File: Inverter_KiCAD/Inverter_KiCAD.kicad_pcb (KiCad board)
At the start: 2 copper layers, 46.8 x 6.8 mm, 139 parts, among them J1 PX0580-PC-12132, J2 Conn_ST_STDC14, J3 Conn_01x04, J4 Conn_01x05, J5 USB_C_Receptacle_USB2.0, Q1 HCPL-315J-500E, Q10 HCPL-315J-500E, Q2 IRF540N, Q3 IRF540N, Q4 IRF540N, Q5 IRF540N, Q6 HCPL-315J-500E, Q7 IRF540N, Q8 IRF540N, Q9 BUK9637-100E, SW1 SW_Push, SW2 SW_Push, SW3 SW_Push, SW4 SW_Push, SW5 SW_Push, U1 MPRB2415S-6W, U10 MPRB2415S-6W, U12 MPRB2415S-6W, U13 MP-LD30-23B12R2, U14 AZ1117-3.3, U15 HCPL-7800A, U16 HCPL-7800A, U17 GO 10-SME/SP3, U18 STM32G474RETx, U19 GO 10-SME/SP3, U2 MPRB2415S-6W, U20 USBLC6-2SC6, U22 ACPL-077L, U3 HCPL-7800A, U4 MPRB2415S-6W, U5 MPRB2415S-6W, U6 GO 10-SME/SP3, U8 HCPL-7800A, U9 GO 10-SME/SP3

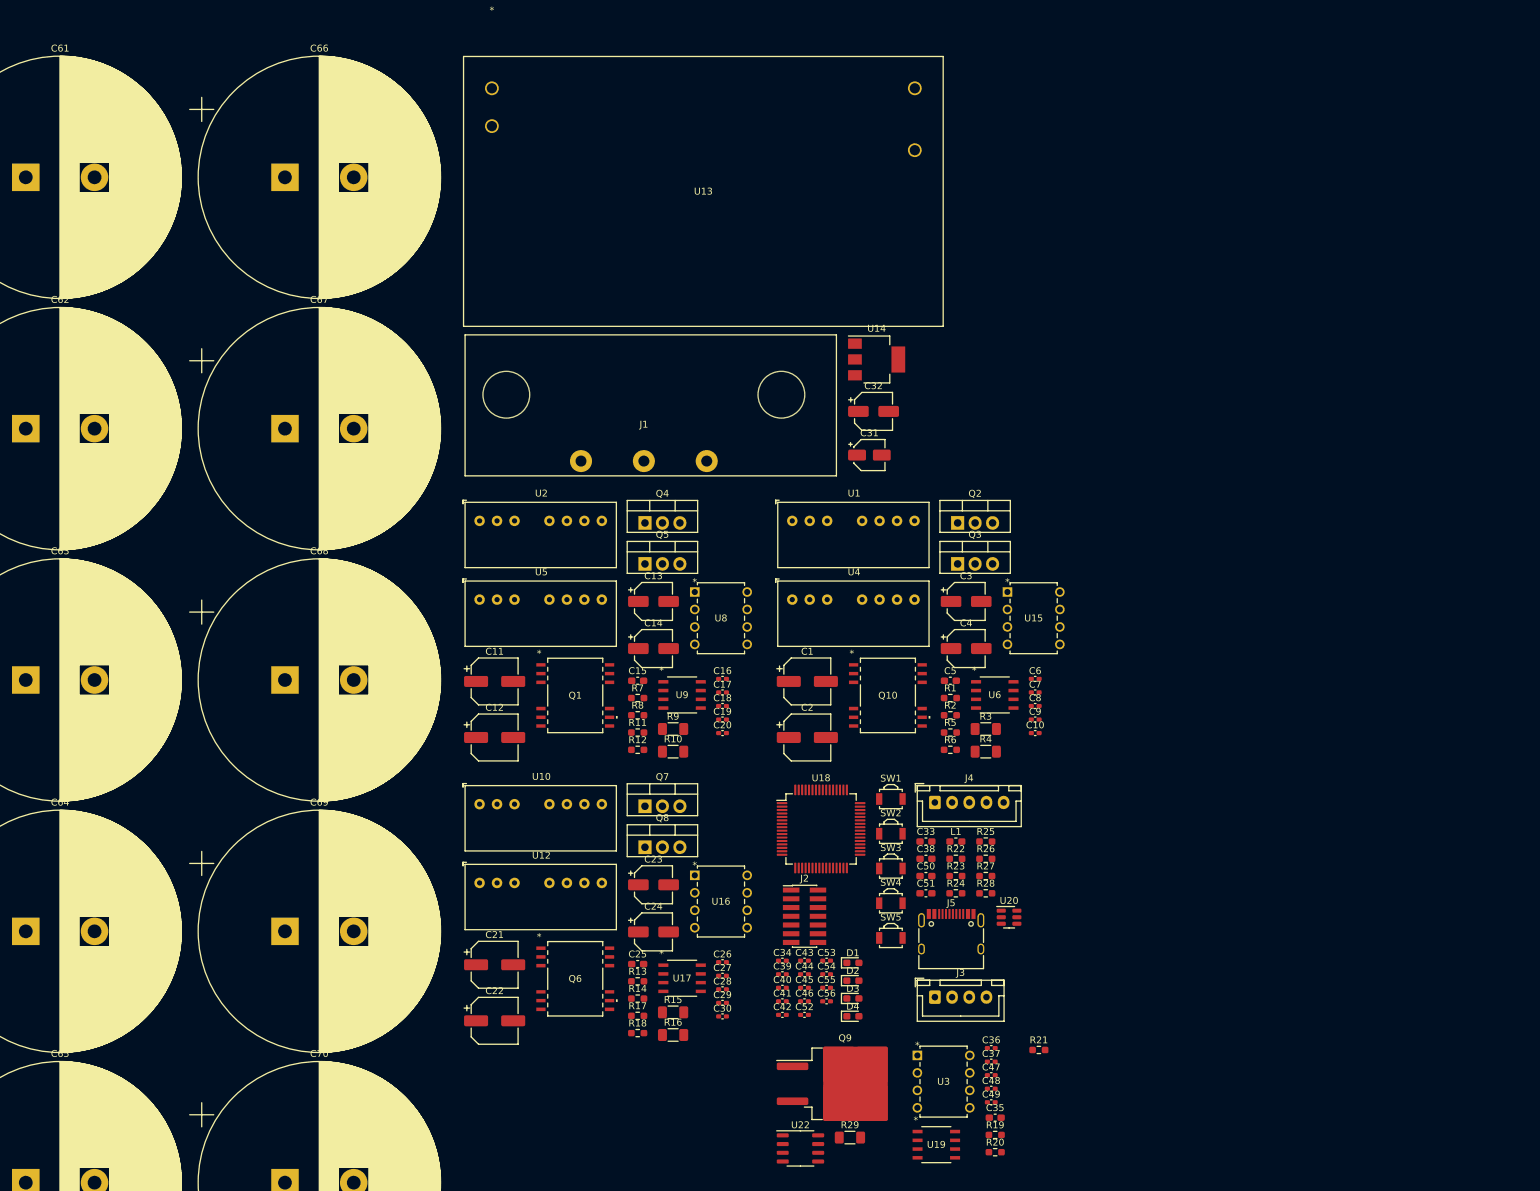
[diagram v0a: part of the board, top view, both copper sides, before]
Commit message: clear schematic errors
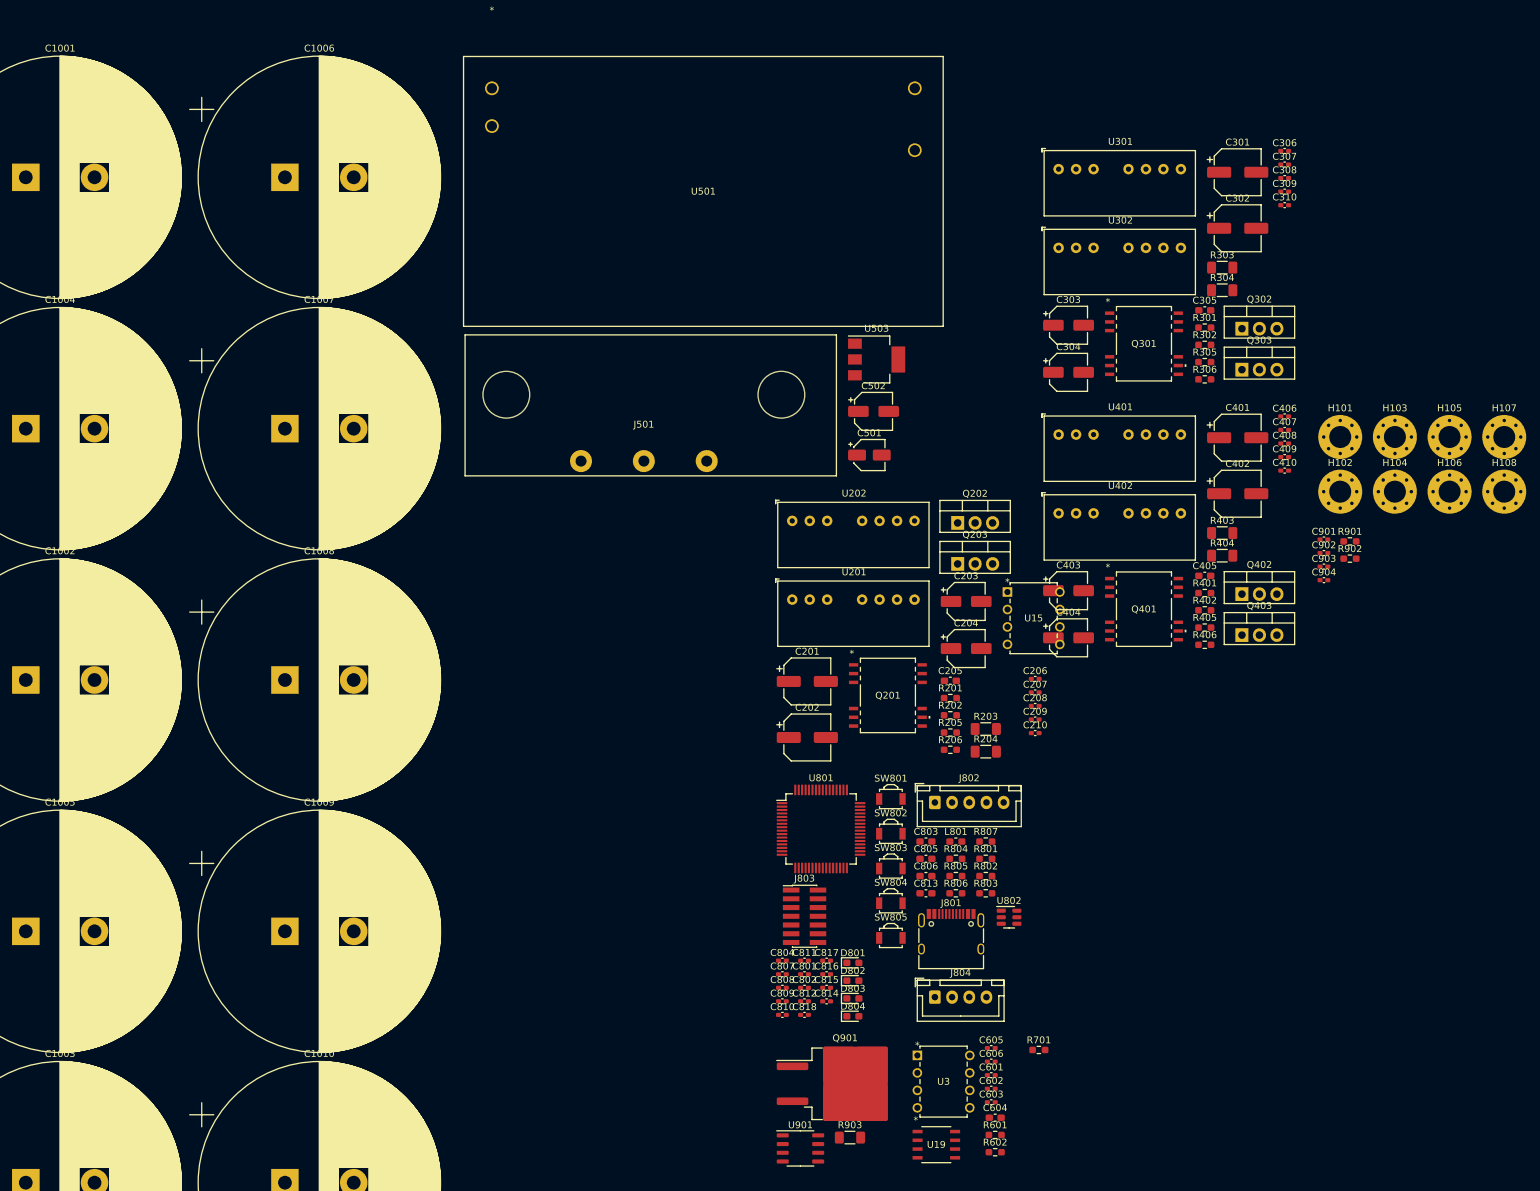
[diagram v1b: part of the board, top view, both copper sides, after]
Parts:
- removed C11, C12, C21, C22: 100u, Capacitor_SMD:CP_Elec_6.3x7.7
- removed C13, C14, C23, C24: 22u, Capacitor_SMD:CP_Elec_5x5.4
- removed C15, C25: C_Small, Capacitor_SMD:C_0603_1608Metric_Pad1.08x0.95mm_HandSolder
- removed C16, C17, C26, C27: 100n, Capacitor_SMD:C_0402_1005Metric_Pad0.74x0.62mm_HandSolder
- removed C18, C19, C20, C28, C29, C30: 4.7n, Capacitor_SMD:C_0402_1005Metric_Pad0.74x0.62mm_HandSolder
- removed Q1, Q6: HCPL-315J-500E, Custom:SO-16_HCPL-315J_BRA
- removed Q4, Q5, Q7, Q8: IRF540N, Package_TO_SOT_THT:TO-220-3_Vertical
- removed R10, R15, R16, R9: 30, Resistor_SMD:R_1206_3216Metric_Pad1.30x1.75mm_HandSolder
- removed R11, R12, R17, R18: R_Small, Resistor_SMD:R_0603_1608Metric_Pad0.98x0.95mm_HandSolder
- removed R13, R14, R7, R8: 170, Resistor_SMD:R_0603_1608Metric_Pad0.98x0.95mm_HandSolder
- removed U10, U12, U2, U5: MPRB2415S-6W, Custom:MPRB2415S
- removed U16, U8: HCPL-7800A, Custom:HCPL-7800A
- removed U17, U6, U9: GO 10-SME/SP3, Custom:SOIC8-GO-SME&slash_SP3_LEM
- added C301: 100u, Capacitor_SMD:CP_Elec_6.3x7.7, F.Cu at (184.9, 27.1)
- added C302: 100u, Capacitor_SMD:CP_Elec_6.3x7.7, F.Cu at (184.9, 35.2)
- added C303: 22u, Capacitor_SMD:CP_Elec_5x5.4, F.Cu at (160.3, 49.3)
- added C304: 22u, Capacitor_SMD:CP_Elec_5x5.4, F.Cu at (160.3, 56.2)
- added C305: 10n, Capacitor_SMD:C_0603_1608Metric_Pad1.08x0.95mm_HandSolder, F.Cu at (180.1, 47.1)
- added C306: 100n, Capacitor_SMD:C_0402_1005Metric_Pad0.74x0.62mm_HandSolder, F.Cu at (191.7, 24.0)
- added C307: 100n, Capacitor_SMD:C_0402_1005Metric_Pad0.74x0.62mm_HandSolder, F.Cu at (191.7, 25.9)
- added C308: 4.7n, Capacitor_SMD:C_0402_1005Metric_Pad0.74x0.62mm_HandSolder, F.Cu at (191.7, 27.9)
- added C309: 4.7n, Capacitor_SMD:C_0402_1005Metric_Pad0.74x0.62mm_HandSolder, F.Cu at (191.7, 29.9)
- added C310: 4.7n, Capacitor_SMD:C_0402_1005Metric_Pad0.74x0.62mm_HandSolder, F.Cu at (191.7, 31.9)
- added C401: 100u, Capacitor_SMD:CP_Elec_6.3x7.7, F.Cu at (184.9, 65.7)
- added C402: 100u, Capacitor_SMD:CP_Elec_6.3x7.7, F.Cu at (184.9, 73.8)
- added C403: 22u, Capacitor_SMD:CP_Elec_5x5.4, F.Cu at (160.3, 87.9)
- added C404: 22u, Capacitor_SMD:CP_Elec_5x5.4, F.Cu at (160.3, 94.8)
- added C405: 10n, Capacitor_SMD:C_0603_1608Metric_Pad1.08x0.95mm_HandSolder, F.Cu at (180.1, 85.7)
- added C406: 100n, Capacitor_SMD:C_0402_1005Metric_Pad0.74x0.62mm_HandSolder, F.Cu at (191.7, 62.6)
- added C407: 100n, Capacitor_SMD:C_0402_1005Metric_Pad0.74x0.62mm_HandSolder, F.Cu at (191.7, 64.5)
- added C408: 4.7n, Capacitor_SMD:C_0402_1005Metric_Pad0.74x0.62mm_HandSolder, F.Cu at (191.7, 66.5)
- added C409: 4.7n, Capacitor_SMD:C_0402_1005Metric_Pad0.74x0.62mm_HandSolder, F.Cu at (191.7, 68.5)
- added C410: 4.7n, Capacitor_SMD:C_0402_1005Metric_Pad0.74x0.62mm_HandSolder, F.Cu at (191.7, 70.5)
- added C901: 100n, Capacitor_SMD:C_0402_1005Metric_Pad0.74x0.62mm_HandSolder, F.Cu at (197.4, 80.5)
- added C902: 100n, Capacitor_SMD:C_0402_1005Metric_Pad0.74x0.62mm_HandSolder, F.Cu at (197.4, 82.4)
- added C903: 1u, Capacitor_SMD:C_0402_1005Metric_Pad0.74x0.62mm_HandSolder, F.Cu at (197.4, 84.4)
- added C904: 1n, Capacitor_SMD:C_0402_1005Metric_Pad0.74x0.62mm_HandSolder, F.Cu at (197.4, 86.4)
- added H101: MountingHole_Pad, MountingHole:MountingHole_3.2mm_M3_Pad_Via, F.Cu at (199.8, 65.6)
- added H102: MountingHole_Pad, MountingHole:MountingHole_3.2mm_M3_Pad_Via, F.Cu at (199.8, 73.5)
- added H103: MountingHole_Pad, MountingHole:MountingHole_3.2mm_M3_Pad_Via, F.Cu at (207.8, 65.6)
- added H104: MountingHole_Pad, MountingHole:MountingHole_3.2mm_M3_Pad_Via, F.Cu at (207.8, 73.5)
- added H105: MountingHole_Pad, MountingHole:MountingHole_3.2mm_M3_Pad_Via, F.Cu at (215.7, 65.6)
- added H106: MountingHole_Pad, MountingHole:MountingHole_3.2mm_M3_Pad_Via, F.Cu at (215.7, 73.5)
- added H107: MountingHole_Pad, MountingHole:MountingHole_3.2mm_M3_Pad_Via, F.Cu at (223.7, 65.6)
- added H108: MountingHole_Pad, MountingHole:MountingHole_3.2mm_M3_Pad_Via, F.Cu at (223.7, 73.5)
- added Q301: HCPL-315J-500E, Custom:SO-16_HCPL-315J_BRA, F.Cu at (171.3, 52.0)
- added Q302: IRF540N, Package_TO_SOT_THT:TO-220-3_Vertical, F.Cu at (185.5, 49.8)
- added Q303: IRF540N, Package_TO_SOT_THT:TO-220-3_Vertical, F.Cu at (185.5, 55.8)
- added Q401: HCPL-315J-500E, Custom:SO-16_HCPL-315J_BRA, F.Cu at (171.3, 90.6)
- added Q402: IRF540N, Package_TO_SOT_THT:TO-220-3_Vertical, F.Cu at (185.5, 88.4)
- added Q403: IRF540N, Package_TO_SOT_THT:TO-220-3_Vertical, F.Cu at (185.5, 94.4)
- added R301: 170, Resistor_SMD:R_0603_1608Metric_Pad0.98x0.95mm_HandSolder, F.Cu at (180.1, 49.7)
- added R302: 170, Resistor_SMD:R_0603_1608Metric_Pad0.98x0.95mm_HandSolder, F.Cu at (180.1, 52.2)
- added R303: 30, Resistor_SMD:R_1206_3216Metric_Pad1.30x1.75mm_HandSolder, F.Cu at (182.7, 40.9)
- added R304: 30, Resistor_SMD:R_1206_3216Metric_Pad1.30x1.75mm_HandSolder, F.Cu at (182.7, 44.2)
- added R305: 160k, Resistor_SMD:R_0603_1608Metric_Pad0.98x0.95mm_HandSolder, F.Cu at (180.1, 54.7)
- added R306: 1k, Resistor_SMD:R_0603_1608Metric_Pad0.98x0.95mm_HandSolder, F.Cu at (180.1, 57.2)
- added R401: 170, Resistor_SMD:R_0603_1608Metric_Pad0.98x0.95mm_HandSolder, F.Cu at (180.1, 88.3)
- added R402: 170, Resistor_SMD:R_0603_1608Metric_Pad0.98x0.95mm_HandSolder, F.Cu at (180.1, 90.8)
- added R403: 30, Resistor_SMD:R_1206_3216Metric_Pad1.30x1.75mm_HandSolder, F.Cu at (182.7, 79.5)
- added R404: 30, Resistor_SMD:R_1206_3216Metric_Pad1.30x1.75mm_HandSolder, F.Cu at (182.7, 82.8)
- added R405: 160k, Resistor_SMD:R_0603_1608Metric_Pad0.98x0.95mm_HandSolder, F.Cu at (180.1, 93.3)
- added R406: 1k, Resistor_SMD:R_0603_1608Metric_Pad0.98x0.95mm_HandSolder, F.Cu at (180.1, 95.8)
- added R901: 100, Resistor_SMD:R_0603_1608Metric_Pad0.98x0.95mm_HandSolder, F.Cu at (201.2, 80.7)
- added R902: 10k, Resistor_SMD:R_0603_1608Metric_Pad0.98x0.95mm_HandSolder, F.Cu at (201.2, 83.3)
- added U301: MPRB2415S-6W, Custom:MPRB2415S, F.Cu at (167.8, 26.6)
- added U302: MPRB2415S-6W, Custom:MPRB2415S, F.Cu at (167.8, 38.1)
- added U401: MPRB2415S-6W, Custom:MPRB2415S, F.Cu at (167.8, 65.2)
- added U402: MPRB2415S-6W, Custom:MPRB2415S, F.Cu at (167.8, 76.7)
- C205: renamed from C5; value C_Small -> 10n
- C604: renamed from C35; value C_Small -> 10n
- R205: renamed from R5; value R_Small -> 160k
- R206: renamed from R6; value R_Small -> 1k
- R601: renamed from R19; value R_Small -> 160k
- R602: renamed from R20; value R_Small -> 1k
- renumbered C61 to C1001, C63 to C1002, C65 to C1003, C62 to C1004, C64 to C1005, C66 to C1006, C67 to C1007, C68 to C1008, C69 to C1009, C70 to C1010, C1 to C201, C2 to C202, C3 to C203, C4 to C204, C6 to C206, C7 to C207, C8 to C208, C9 to C209, C10 to C210, C31 to C501, C32 to C502, C47 to C601, C48 to C602, C49 to C603, C36 to C605, C37 to C606, C44 to C801, C45 to C802, C33 to C803, C34 to C804, C38 to C805, C50 to C806, C39 to C807, C40 to C808, C41 to C809, C42 to C810, C43 to C811, C46 to C812, C51 to C813, C56 to C814, C55 to C815, C54 to C816, C53 to C817, C52 to C818, D1 to D801, D2 to D802, D3 to D803, D4 to D804, J1 to J501, J5 to J801, J4 to J802, J2 to J803, J3 to J804, L1 to L801, Q10 to Q201, Q2 to Q202, Q3 to Q203, Q9 to Q901, R1 to R201, R2 to R202, R3 to R203, R4 to R204, R21 to R701, R26 to R801, R27 to R802, R28 to R803, R22 to R804, R23 to R805, R24 to R806, R25 to R807, R29 to R903, SW1 to SW801, SW2 to SW802, SW3 to SW803, SW4 to SW804, SW5 to SW805, U4 to U201, U1 to U202, U13 to U501, U14 to U503, U18 to U801, U20 to U802, U22 to U901
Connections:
- net /MCU_STM32G474/Nucleo_Rx renamed /NUCLEO_TX
- net /MCU_STM32G474/Nucleo_Tx renamed /NUCLEO_RX
- C205 pad 1: Net-(U15-VIN+) -> Net-(U203-VIN+)
- C604 pad 1: Net-(U3-VIN+) -> Net-(U602-VIN+)
- R205 pad 1: /Arm_IRF540NBbF/V_Out -> /U_output
- R205 pad 2: Net-(U15-VIN+) -> Net-(U203-VIN+)
- R206 pad 1: Net-(U15-VIN+) -> Net-(U203-VIN+)
- R601 pad 2: Net-(U3-VIN+) -> Net-(U602-VIN+)
- R602 pad 1: Net-(U3-VIN+) -> Net-(U602-VIN+)

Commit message: end of sch, start pcb
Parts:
- removed U15, U3: HCPL-7800A, Custom:HCPL-7800A
- added C1201: 100n, Capacitor_SMD:C_0402_1005Metric_Pad0.74x0.62mm_HandSolder, F.Cu at (-58.4, 163.0)
- added D901: Red, LED_SMD:LED_0603_1608Metric_Pad1.05x0.95mm_HandSolder, F.Cu at (-80.9, 181.3)
- added D902: VS-15TQ060S-M3, Package_TO_SOT_SMD:TO-263-2, F.Cu at (-80.8, 173.8)
- added F501: Fuse, Custom:0031.8201, F.Cu at (-78.4, 149.2)
- added J101: Conn_02x19_Odd_Even, Connector_PinHeader_2.54mm:PinHeader_2x19_P2.54mm_Vertical, F.Cu at (-120.0, 146.2)
- added J103: Conn_02x19_Odd_Even, Connector_PinHeader_2.54mm:PinHeader_2x19_P2.54mm_Vertical, F.Cu at (-98.4, 145.3)
- added J1101: Conn_01x02, Connector_JST:JST_XH_B2B-XH-A_1x02_P2.50mm_Vertical, F.Cu at (-55.7, 171.0)
- added J1102: Conn_01x02, Connector_JST:JST_XH_B2B-XH-A_1x02_P2.50mm_Vertical, F.Cu at (-55.7, 178.8)
- added Q1101: SQ2310ES, Package_TO_SOT_SMD:SOT-23, F.Cu at (-47.3, 169.8)
- added R1101: 22, Resistor_SMD:R_0402_1005Metric_Pad0.72x0.64mm_HandSolder, F.Cu at (-48.1, 173.1)
- added R1102: 10k, Resistor_SMD:R_0402_1005Metric_Pad0.72x0.64mm_HandSolder, F.Cu at (-48.1, 175.0)
- added R1201: 200, Resistor_SMD:R_0402_1005Metric_Pad0.72x0.64mm_HandSolder, F.Cu at (-61.6, 163.0)
- added U1201: TCN75A, Package_SO:SOIC-8_3.9x4.9mm_P1.27mm, F.Cu at (-59.0, 158.8)
- added U203: HCPL-7800A, Custom:HCPL-7800A, F.Cu at (-70.3, 190.0)
- added U204: GO 10-SME/SP3, Custom:SOIC8-GO-SME&slash_SP3_LEM, F.Cu at (-67.6, 203.0)
- added U303: HCPL-7800A, Custom:HCPL-7800A, F.Cu at (-90.0, 190.5)
- added U304: GO 10-SME/SP3, Custom:SOIC8-GO-SME&slash_SP3_LEM, F.Cu at (-87.3, 203.4)
- added U403: HCPL-7800A, Custom:HCPL-7800A, F.Cu at (-70.3, 169.7)
- added U404: GO 10-SME/SP3, Custom:SOIC8-GO-SME&slash_SP3_LEM, F.Cu at (-67.6, 182.6)
- added U502: 173010542, Custom:173010578, F.Cu at (-87.4, 158.3)
- added U602: HCPL-7800A, Custom:HCPL-7800A, F.Cu at (-57.6, 195.6)
- added U701: 17791063215, Custom:17791063215, F.Cu at (-51.6, 148.3)
- added U902: TC1412, Package_SO:SOIC-8_3.9x4.9mm_P1.27mm, F.Cu at (-87.3, 183.2)
- added Y801: 16M, Custom:ABLS-7.3728MHZ-CL-RESR-A-1-G-F, F.Cu at (-51.5, 188.4)
- C205, C305, C405, C604, C805: footprint Capacitor_SMD:C_0603_1608Metric_Pad1.08x0.95mm_HandSolder -> Capacitor_SMD:C_0402_1005Metric_Pad0.74x0.62mm_HandSolder
- R201, R202, R205, R206, R301, R302, R305, R306, R401, R402, R405, R406, R601, R602, R701, R801, R802, R803, R804, R805, R806, R807, R901, R902: footprint Resistor_SMD:R_0603_1608Metric_Pad0.98x0.95mm_HandSolder -> Resistor_SMD:R_0402_1005Metric_Pad0.72x0.64mm_HandSolder
- moved C1001 380.5 mm to (382.2, -44.7)
- moved C1002 380.5 mm to (382.2, 28.4)
- moved C1003 380.5 mm to (382.2, 101.5)
- moved C1004 380.5 mm to (382.2, -8.14)
- moved C1005 380.5 mm to (382.2, 65.0)
- moved C1006 380.5 mm to (419.9, -44.7)
- moved C1007 380.5 mm to (419.9, -8.14)
- moved C1008 380.5 mm to (419.9, 28.4)
- moved C1009 380.5 mm to (419.9, 65.0)
- moved C1010 380.5 mm to (419.9, 101.5)
- moved J501 243.8 mm to (-118.9, -46.0)
- moved H101 236.2 mm to (-35.6, 46.6)
- moved H102 236.2 mm to (-35.6, 54.6)
- moved H103 236.2 mm to (-27.6, 46.6)
- moved H104 236.2 mm to (-27.6, 54.6)
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- renumbered U19 to U601
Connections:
- net /MCU_STM32G474/Screen_SCL renamed /I2C_SCL
- net /MCU_STM32G474/Screen_SDA renamed /I2C_SDA
- U801 pad 18: unconnected-(U801-PA4-Pad18) -> /MCU_STM32G474/USR_BTN_2
- U801 pad 57: /MCU_STM32G474/USR_BTN_2 -> /ISO_PWM_FAN

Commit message: rooting done
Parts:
- removed the C1001 at (382.2, -44.7)
- added J102: Conn_01x03, Custom:691311700003, F.Cu at (38.0, 97.0)
- added J104: Conn_01x04, Custom:691311700004, F.Cu at (211.0, 92.5)
- added J901: Conn_01x02, Custom:691311700002, F.Cu at (38.0, 83.5)
- C205, C206, C207, C208, C209, C210, C305, C306, C307, C308, C309, C310, C405, C406, C407, C408, C409, C410, R205, R206, R305, R306, R405, R406, U204, U304, U404: moved to B.Cu
- SW801, SW802, SW803, SW804, SW805: footprint Button_Switch_SMD:SW_SPST_B3U-3000P -> Custom:435451019820
- U203, U303, U403: value HCPL-7800A -> HCPL-7800-500E; footprint Custom:HCPL-7800A -> Custom:DIP-8 Gull Wing; moved to B.Cu
- U602: value HCPL-7800A -> HCPL-7800-500E; footprint Custom:HCPL-7800A -> Custom:DIP-8 Gull Wing
- moved C1005 376.3 mm to (53.0, 39.0), turned to 90 degrees
- moved C1006 334.2 mm to (89.0, 39.0), turned to 90 degrees
- moved H108 328.3 mm to (37.0, 72.0)
- moved C1003 318.6 mm to (71.0, 59.9), turned to -90 degrees
- moved H105 311.4 mm to (37.0, 18.0)
- moved Q302 307.0 mm to (135.1, 102.9)
- moved J101 305.7 mm to (185.3, 130.6), turned to -90 degrees
- moved Q303 295.3 mm to (146.1, 102.9)
- moved C1007 295.1 mm to (125.0, 39.0), turned to 90 degrees
- moved U501 294.6 mm to (74.0, 194.8), turned to 90 degrees
- moved Q202 290.9 mm to (87.5, 102.9)
- moved J103 287.4 mm to (185.3, 191.5), turned to -90 degrees
- moved H103 283.2 mm to (213.0, 196.0)
- moved Q203 278.9 mm to (98.5, 102.9)
- moved C1001 277.0 mm to (107.0, 59.9), turned to -90 degrees
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- renumbered C1002 to C1001, C1003 to C1002, C1004 to C1003, C1005 to C1004, C1006 to C1005, C1007 to C1006, C1008 to C1007, C1009 to C1008, C1010 to C1009, D803 to locked
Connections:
- J801 pad S1: unconnected-(J801-SHIELD-PadS1) -> /ISO_GND
- Q901 pad 2: Net-(J901-Pin_2) -> /break/Break_Drain_Mosfet
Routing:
- net /ISO_3V3: track 0.00 -> 378.1 mm, vias 0 -> 17
- net /ISO_15V: track 0.00 -> 223.6 mm
- net /ISO_5V: track 0.00 -> 216.7 mm, vias 0 -> 7
- net /Pwr_En: track 0.00 -> 208.9 mm, vias 0 -> 3
- net /5V: track 0.00 -> 166.9 mm, vias 0 -> 3
- net /Bus_Imes: track 0.00 -> 161.3 mm, vias 0 -> 4
- net /Bus_V: track 0.00 -> 160.3 mm, vias 0 -> 6
- net /V_PWM_L: track 0.00 -> 142.4 mm, vias 0 -> 3
- net /U_output: track 0.00 -> 142.1 mm
- net /V_PWM_H: track 0.00 -> 135.6 mm, vias 0 -> 3
- net /ISO_PWM_Break: track 0.00 -> 129.4 mm, vias 0 -> 2
- net /U_PWM_L: track 0.00 -> 126.4 mm, vias 0 -> 4
- net /U_PWM_H: track 0.00 -> 125.3 mm, vias 0 -> 3
- net /U_Imes: track 0.00 -> 108.8 mm, vias 0 -> 5
- net /W_VPh: track 0.00 -> 108.0 mm, vias 0 -> 3
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- added copper zone on B.Cu, net /ISO_GND
- added copper zone on F.Cu, net /ISO_GND
- added copper zone on B.Cu, net /VSupply_AB
- added copper zone on F.Cu, net /VSupply_AB
- added copper zone on B.Cu, net /Vbus
- added copper zone on F.Cu, net /Vbus
- added copper zone on B.Cu, net GND
- added copper zone on F.Cu, net GND
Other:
- board size 46.8 x 6.8 mm -> 184 x 186 mm
- board text added: "U201"
